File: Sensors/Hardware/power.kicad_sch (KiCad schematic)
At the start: 38 parts, among them J11 Conn_01x02_Male, U12 MAX40200AUK, U19 TPS61222DCK, U8 TPS63031

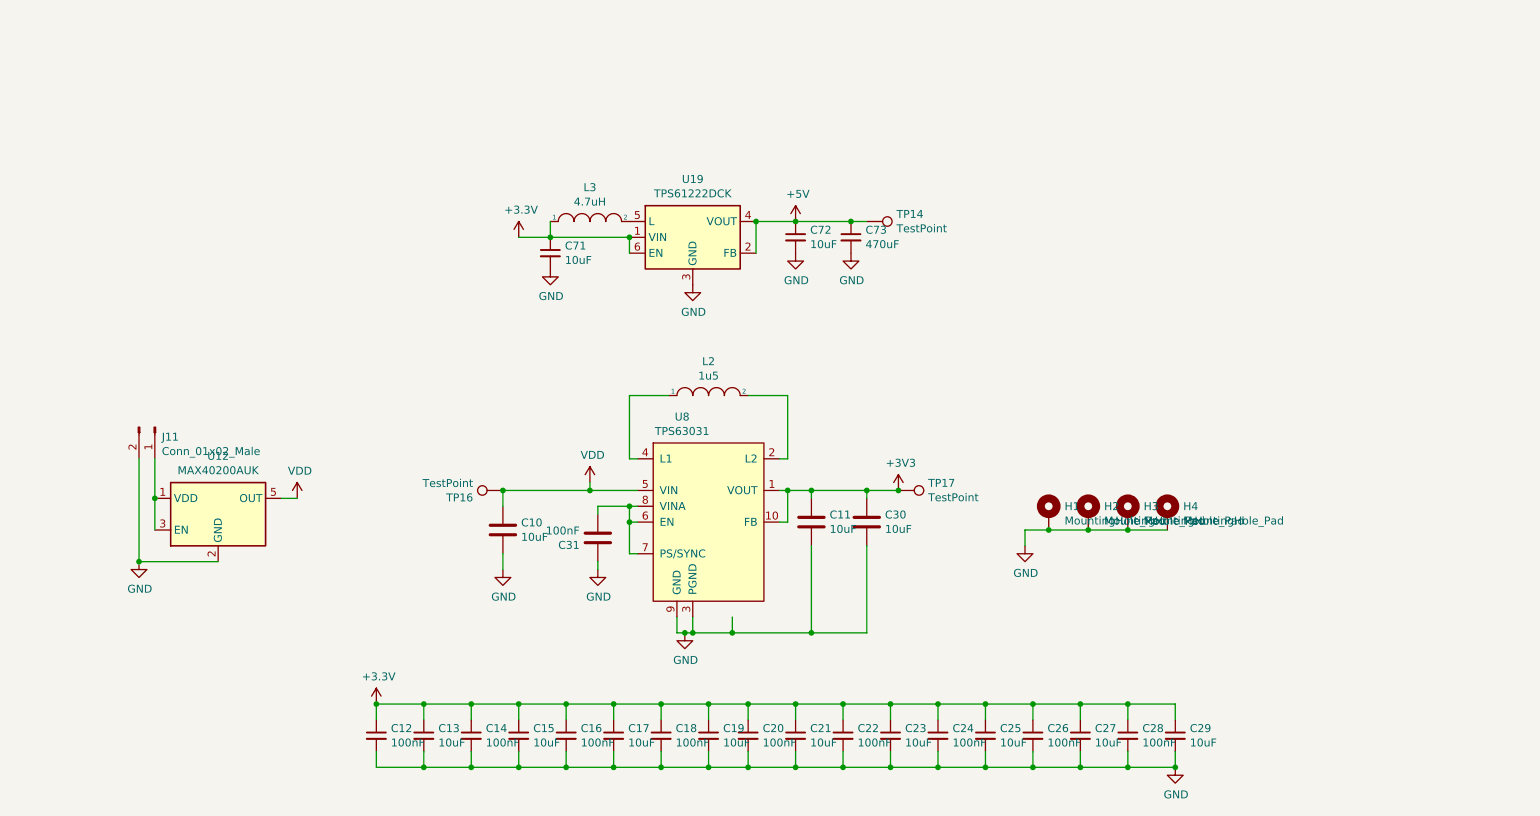
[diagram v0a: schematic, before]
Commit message: added template changes
Moved power to seperate file
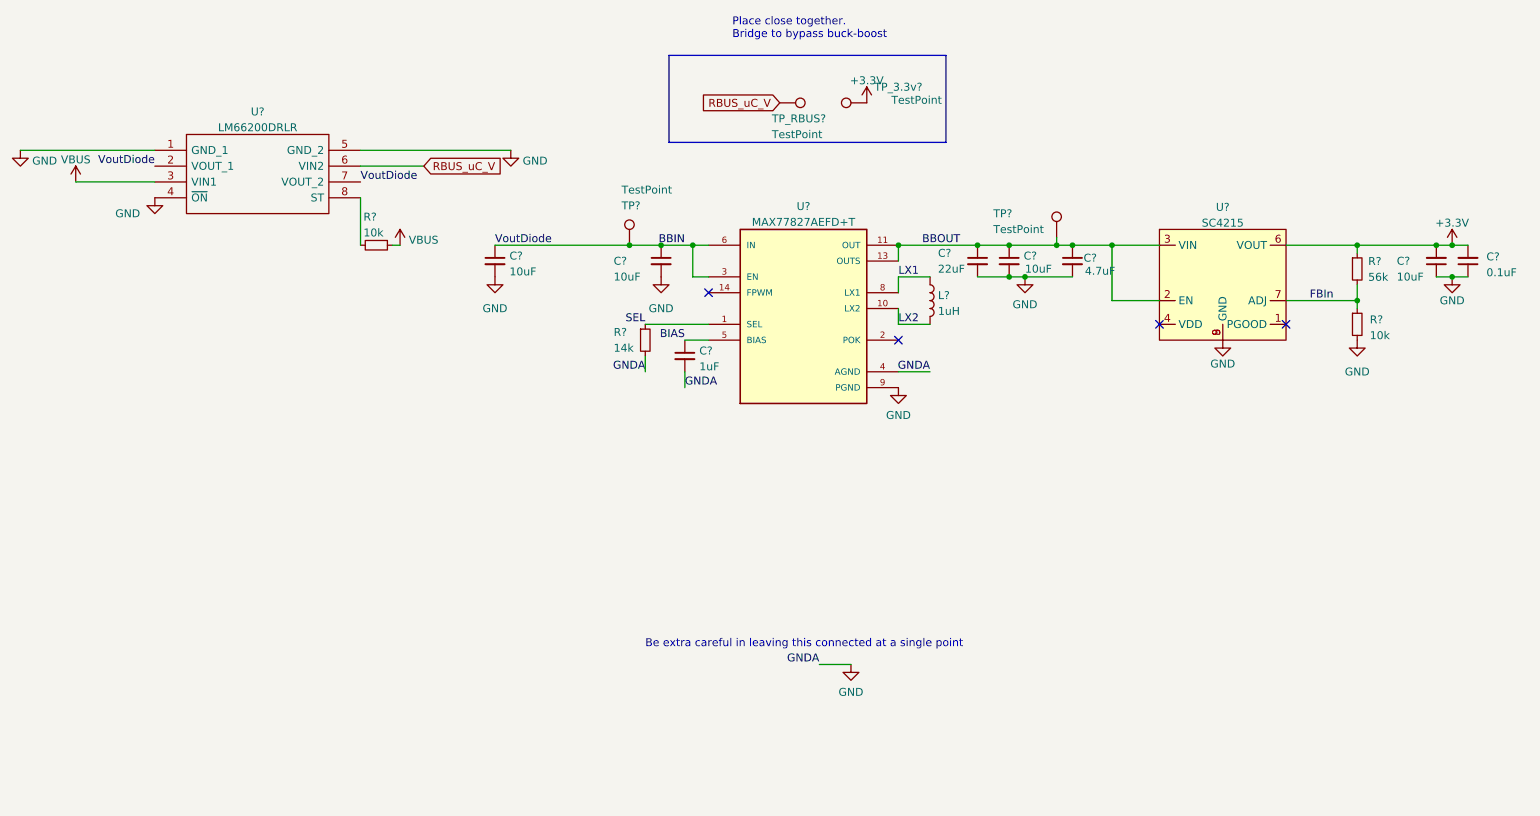
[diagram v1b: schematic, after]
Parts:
- removed C10, C11, C30: 10uF, Capacitor_SMD:C_0603_1608Metric, symbol Device:C
- removed C12, C14, C16, C18, C20, C22, C24, C26, C28: 100nF, Capacitor_SMD:C_0603_1608Metric, symbol Device:C_Small
- removed C13, C15, C17, C19, C21, C23, C25, C27, C29, C71, C72: 10uF, Capacitor_SMD:C_0603_1608Metric, symbol Device:C_Small
- removed C31: 100nF, Capacitor_SMD:C_0603_1608Metric, symbol Device:C
- removed C73: 470uF, Capacitor_SMD:C_0603_1608Metric, symbol Device:C_Small
- removed H1, H2, H3, H4: MountingHole_Pad, MountingHole:MountingHole_3.2mm_M3_DIN965_Pad, symbol Mechanical:MountingHole_Pad
- removed J11: Conn_01x02_Male, Connector_JST:JST_PH_S2B-PH-K_1x02_P2.00mm_Horizontal, symbol Connector:Conn_01x02_Male
- removed L2: 1u5, Inductor_SMD:L_Taiyo-Yuden_NR-30xx, symbol pspice:INDUCTOR
- removed L3: 4.7uH, symbol pspice:INDUCTOR
- removed TP14, TP16, TP17: TestPoint, TestPoint:TestPoint_Pad_D1.0mm, symbol Connector:TestPoint
- removed U12: MAX40200AUK, Package_TO_SOT_SMD:SOT-23-5, symbol Analog_Switch:MAX40200AUK
- removed U19: TPS61222DCK, Package_TO_SOT_SMD:Texas_R-PDSO-G6, symbol Regulator_Switching:TPS61222DCK
- removed U8: TPS63031, iclr-hw:VSON-10-1EP_2.5x2.5mm_Pitch0.5mm_ThermalPad, symbol Mainboard-rescue:TPS63031-iclr
- added C?: 0.1uF, Capacitor_SMD:C_0402_1005Metric, symbol Device:C_Small
- added C?: 4.7uF, Capacitor_SMD:C_0402_1005Metric, symbol Device:C_Small
- added C?: 1uF, Capacitor_SMD:C_0402_1005Metric, symbol Device:C_Small
- added C?: 22uF, Capacitor_SMD:C_0603_1608Metric, symbol Device:C_Small
- added C? (x3): 10uF, Capacitor_SMD:C_0402_1005Metric, symbol Device:C_Small
- added C?: 10uF, Capacitor_SMD:C_0603_1608Metric, symbol Device:C_Small
- added L?: 1uH, Inductor_SMD:L_0805_2012Metric, symbol Device:L
- added R?: 14k, Resistor_SMD:R_0402_1005Metric, symbol Device:R_Small
- added R? (x2): 10k, Resistor_SMD:R_0402_1005Metric, symbol Device:R_Small
- added R?: 56k, Resistor_SMD:R_0402_1005Metric, symbol Device:R_Small
- added TP? (x2), TP_3.3v?, TP_RBUS?: TestPoint, TestPoint:TestPoint_Pad_D1.5mm, symbol Connector:TestPoint
- added U?: MAX77827AEFD+T, iclr:CONV_MAX77827AEFD+T, symbol iclr:MAX77827AEFD+T
- added U?: LM66200DRLR, SOTFL50P160X60-8N, symbol iclr:LM66200DRLR
- added U?: SC4215, iclr:SOIC127P599X175-9N, symbol iclr:RT9025-25GSP
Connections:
- net +3V3: now also C?.2, C?.2, R?.1, TP_3.3v?.1, U?.6 (VOUT)
- net GND: now also C?.1, C?.1, C?.2, C?.2, C?.2, C?.2, C?.2, C?.2, R?.2, R?.2, U?.1 (GND_1), U?.4 (AGND), U?.4 (~{ON}), U?.5 (GND_2), U?.8 (GND), U?.9 (GND), U?.9 (PGND)
- new net: R?.2, U?.8 (ST)
- new net BBIN: C?.1, C?.1, TP?.1, U?.2 (VOUT_1), U?.3 (EN), U?.6 (IN), U?.7 (VOUT_2)
- new net BBOUT: C?.1, C?.1, C?.1, TP?.1, U?.11 (OUT), U?.13 (OUTS), U?.2 (EN), U?.3 (VIN)
- new net BIAS: C?.1, U?.5 (BIAS)
- new net FBIn: R?.1, R?.2, U?.7 (ADJ)
- new net LX1: L?.1, U?.8 (LX1)
- new net LX2: L?.2, U?.10 (LX2)
- new net RBUS_uC_V: TP_RBUS?.1, U?.6 (VIN2)
- new net SEL: R?.1, U?.1 (SEL)
- new net VBUS: R?.1, U?.3 (VIN1)
- no-connect marks 0 -> 4
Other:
- note added: "Be extra careful in leaving this connected at a single point"
- note added: "Place close together. Bridge to bypass buck-boost"

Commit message: fp assignments
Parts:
- C32: renamed from C?; footprint Capacitor_SMD:C_0603_1608Metric -> Capacitor_SMD:C_0402_1005Metric
- TP1, TP2: renamed from TP?; footprint TestPoint:TestPoint_Pad_D1.5mm -> TestPoint:TestPoint_Pad_D1.0mm
- TP_3.3v1: renamed from TP_3.3v?; footprint TestPoint:TestPoint_Pad_D1.5mm -> TestPoint:TestPoint_Pad_D1.0mm
- TP_RBUS1: renamed from TP_RBUS?; footprint TestPoint:TestPoint_Pad_D1.5mm -> TestPoint:TestPoint_Pad_D1.0mm
- U6: renamed from U?; footprint SOTFL50P160X60-8N -> iclr:SOTFL50P160X60-8N
- gave numbers to parts that had none: 14

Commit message: grouping layout
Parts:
- L3: footprint Inductor_SMD:L_0805_2012Metric -> Inductor_SMD:L_0402_1005Metric
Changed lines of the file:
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@@
       (effects (font (size 1.27 1.27)) (justify left))
     )
-    (property "Footprint" "Inductor_SMD:L_0805_2012Metric" (id 2) (at 185.42 66.04 0)
+    (property "Footprint" "Inductor_SMD:L_0402_1005Metric" (id 2) (at 185.42 66.04 0)
       (effects (font (size 1.27 1.27)) hide)
     )

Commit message: power layout done
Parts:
- C32: footprint Capacitor_SMD:C_0402_1005Metric -> Capacitor_SMD:C_0603_1608Metric
- L3: footprint Inductor_SMD:L_0402_1005Metric -> Inductor_SMD:L_0805_2012Metric
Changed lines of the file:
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@@
       (effects (font (size 1.27 1.27)) (justify left))
     )
-    (property "Footprint" "Inductor_SMD:L_0402_1005Metric" (id 2) (at 185.42 66.04 0)
+    (property "Footprint" "Inductor_SMD:L_0805_2012Metric" (id 2) (at 185.42 66.04 0)
       (effects (font (size 1.27 1.27)) hide)
     )
@@
       (effects (font (size 1.27 1.27)) (justify left))
     )
-    (property "Footprint" "Capacitor_SMD:C_0402_1005Metric" (id 2) (at 142.24 59.69 0)
-      (effects (font (size 1.27 1.27)) hide)
-    )
+    (property "Footprint" "Capacitor_SMD:C_0603_1608Metric" (id 2) (at 142.24 59.69 0)
+      (effects (font (size 1.27 1.27)) hide)
+    )

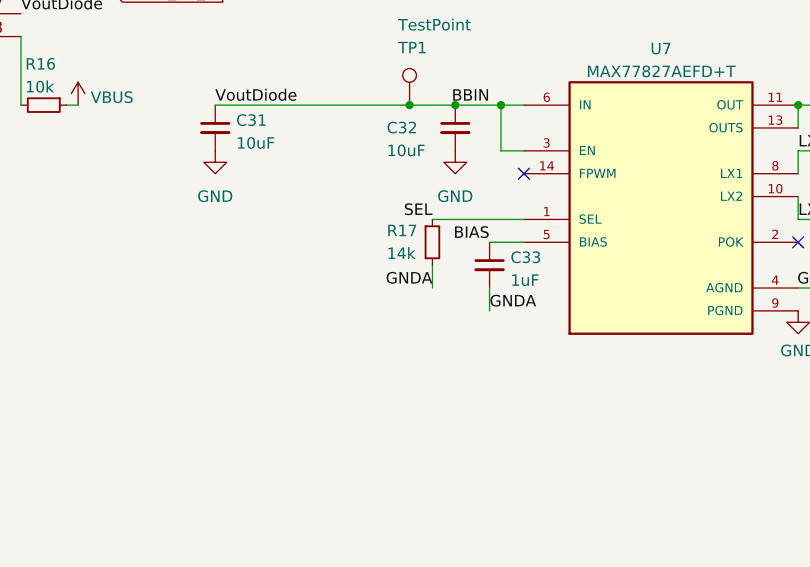
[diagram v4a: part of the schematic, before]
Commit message: esp32 pin rearrangement
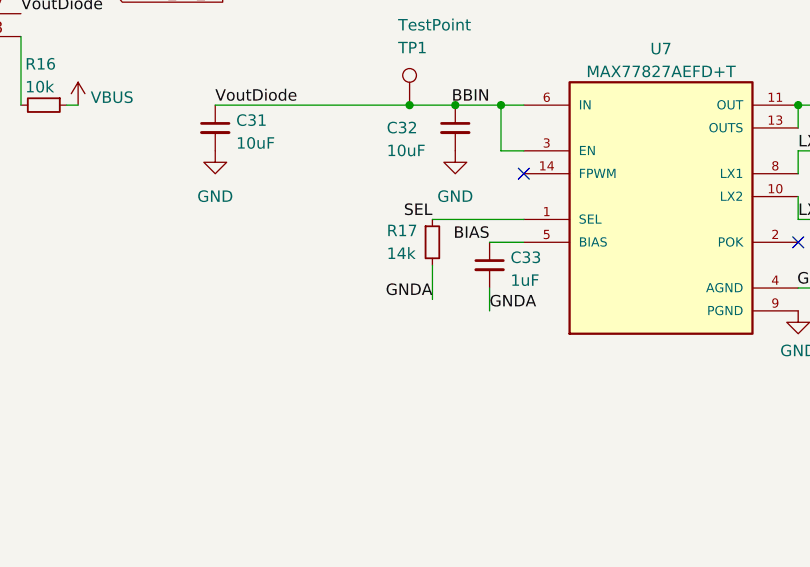
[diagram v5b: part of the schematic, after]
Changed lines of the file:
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@@
     (stroke (width 0) (type default) (color 0 0 0 0))
   )
-  (wire (pts (xy 139.7 77.47) (xy 139.7 74.93))
+  (wire (pts (xy 139.7 78.74) (xy 139.7 74.93))
     (stroke (width 0) (type default) (color 0 0 0 0))
   )
@@
     (effects (font (size 1.27 1.27)) (justify right bottom))
   )
-  (label "GNDA" (at 139.7 77.47 180)
+  (label "GNDA" (at 139.7 78.74 180)
     (effects (font (size 1.27 1.27)) (justify right bottom))
   )

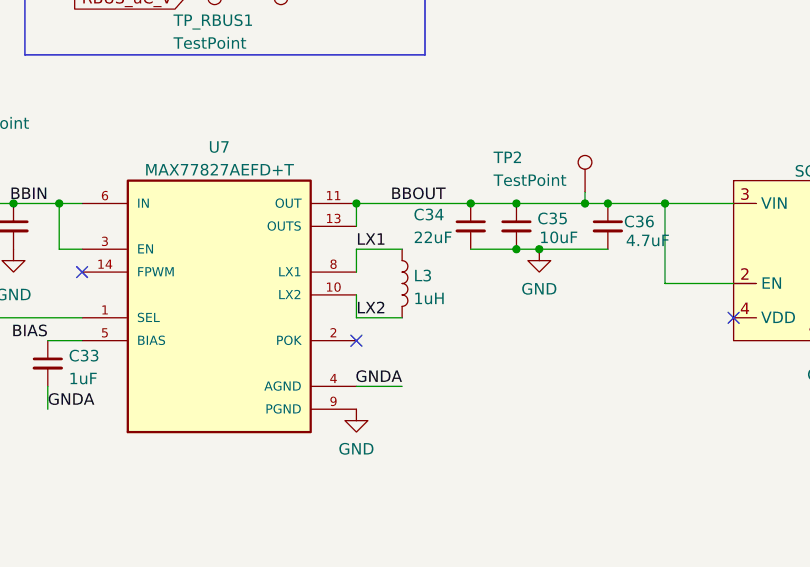
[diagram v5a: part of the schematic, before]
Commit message: ADC connections and KiCAD version update
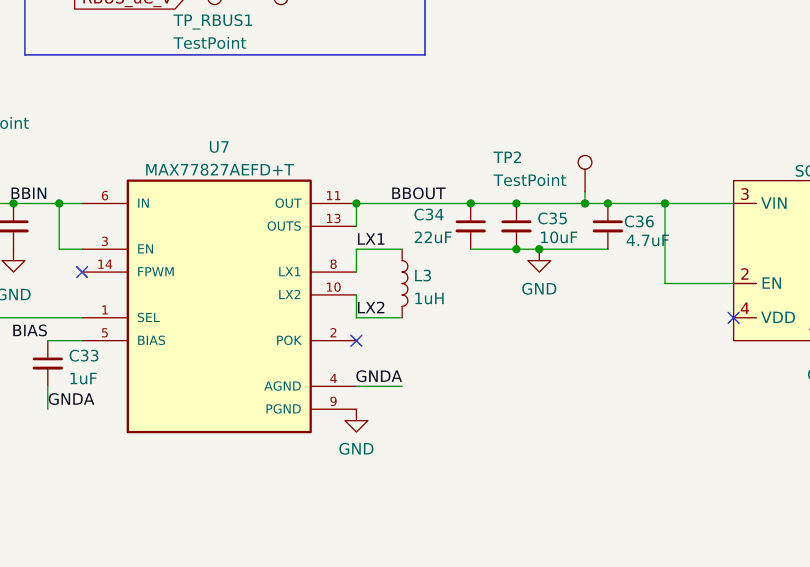
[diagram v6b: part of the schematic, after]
